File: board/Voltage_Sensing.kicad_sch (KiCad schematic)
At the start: 0 parts

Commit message: Schematics without values
Votlage Sensing circuit schematic
Oring controller circuit schematic
No values for components yet
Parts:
- added R10, R11, R12, R13, R14, R15, R16, R17, R18, R19, R20, R21, R22, R23, R24, R25, R26, R3, R4, R5, R6, R7, R8, R9: R_US, symbol Device:R_US
- added U4, U5, U6, U7, U8, U9: Opamp_Dual, symbol Device:Opamp_Dual
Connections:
- new net: R3.1, R4.2, U4.2 (-), U4.6 (-)
- new net: R13.1, R14.1, U6.3 (+)
- new net: R20.1, R22.1, U8.3 (+)
- new net: R23.1, R25.2, U9.2 (-)
- new net: R24.1, R26.1, U9.3 (+)
- new net: R7.1, R8.2, U5.2 (-)
- new net: R5.1, R6.1, U4.3 (+), U4.5 (+)
- new net: R10.1, R9.1, U5.3 (+)
- new net: R11.1, R12.2, U6.2 (-)
- new net: R19.1, R21.2, U8.2 (-)
- new net: R16.1, R17.1, U7.3 (+)
- new net: R15.1, R18.2, U7.2 (-)
- new net Cell_1: R5.2, R7.2
- new net Cell_2: R11.2, R9.2
- new net Cell_3: R13.2, R15.2
- new net Cell_4: R16.2, R19.2
- new net Cell_5: R20.2, R23.2
- new net Cell_6: R24.2
- new net Cell_Sense_1: R4.1, U4.1, U4.7
- new net Cell_Sense_2: R8.1, U5.1
- new net Cell_Sense_3: R12.1, U6.1
- new net Cell_Sense_4: R18.1, U7.1
- new net Cell_Sense_5: R21.1, U8.1
- new net Cell_Sense_6: R25.1, U9.1
- new net GND: R10.2, R14.2, R17.2, R22.2, R26.2, R3.2, R6.2

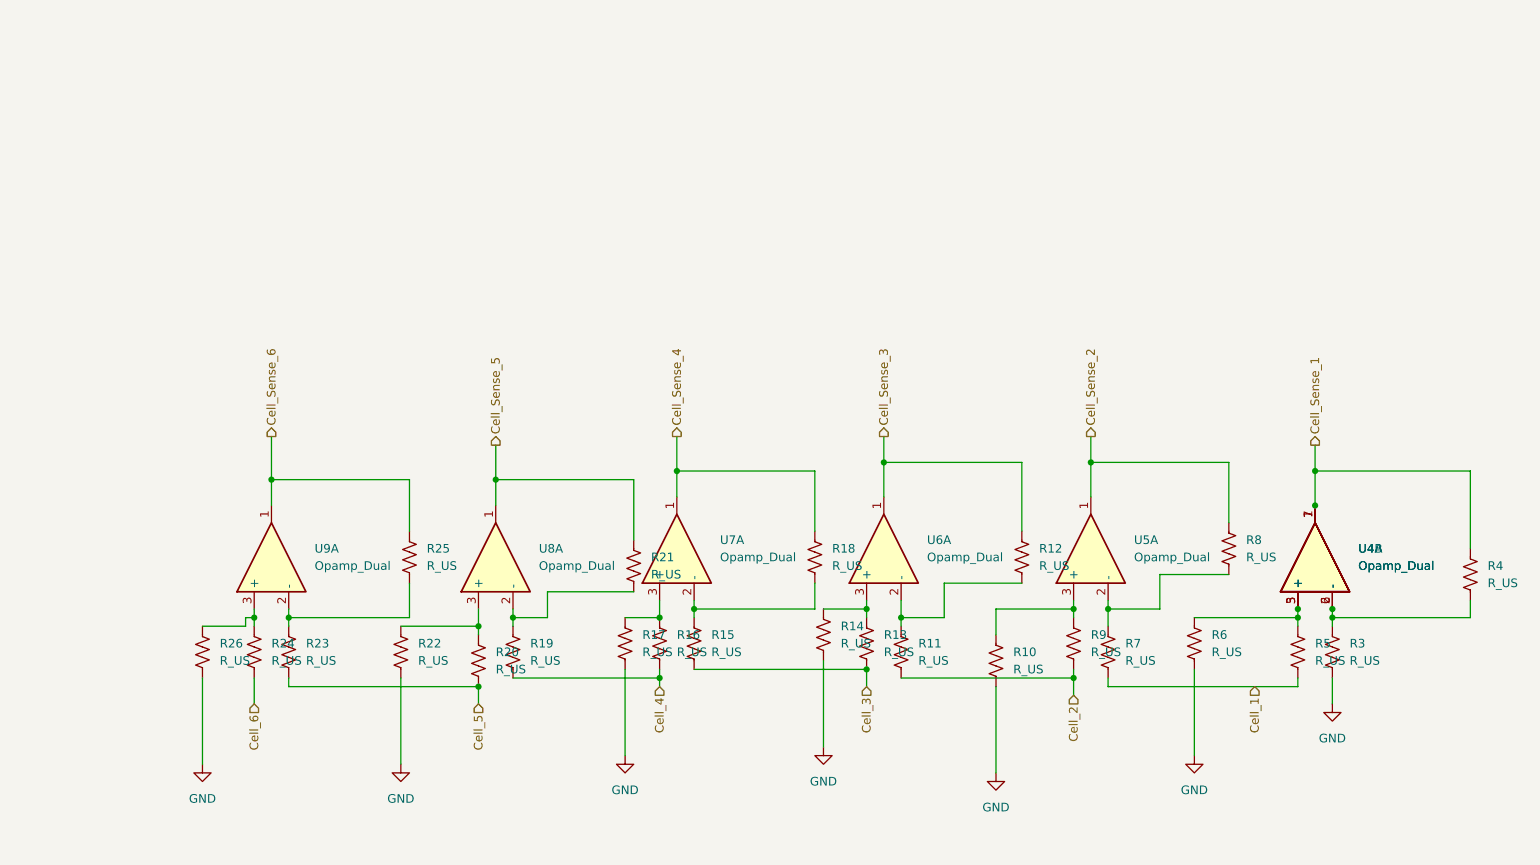
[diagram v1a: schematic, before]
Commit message: Added Zener DIodes
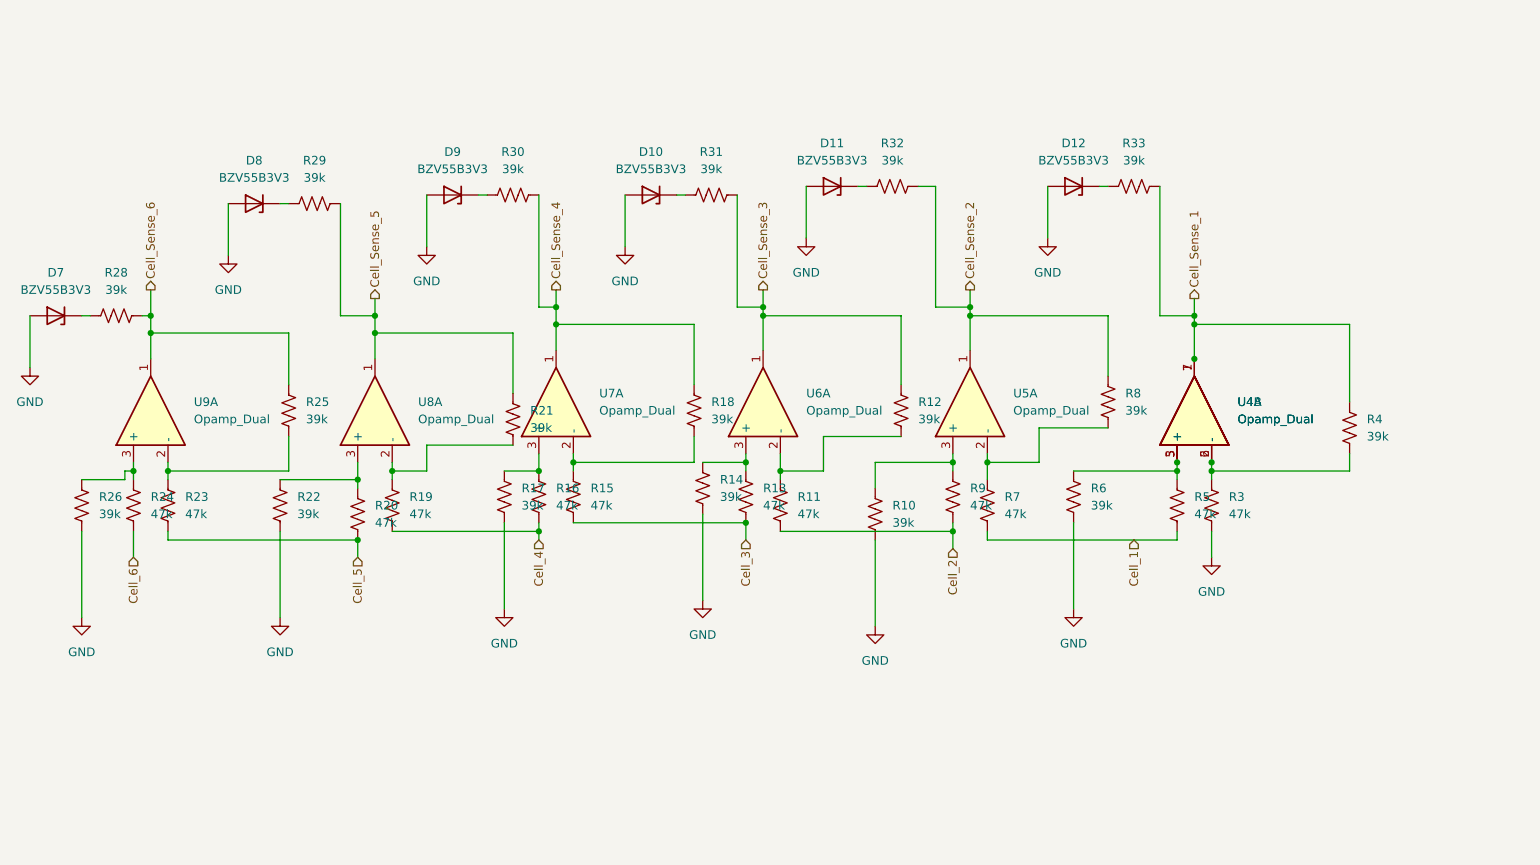
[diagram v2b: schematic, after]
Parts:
- added D10, D11, D12, D7, D8, D9: BZV55B3V3, Diode_SMD:D_MiniMELF, symbol Diode:BZV55B3V3
- added R28, R29, R30, R31, R32, R33: 39k, symbol Device:R_US
- R10, R12, R14, R17, R18, R21, R22, R25, R26, R4, R6, R8: value R_US -> 39k
- R11, R13, R15, R16, R19, R20, R23, R24, R3, R5, R7, R9: value R_US -> 47k
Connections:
- net Cell_Sense_1: now also R33.2
- net Cell_Sense_2: now also R32.2
- net Cell_Sense_3: now also R31.2
- net Cell_Sense_4: now also R30.2
- net Cell_Sense_5: now also R29.2
- net Cell_Sense_6: now also R28.2
- net GND: now also D10.2 (A), D11.2 (A), D12.2 (A), D7.2 (A), D8.2 (A), D9.2 (A)
- new net: D12.1 (K), R33.1
- new net: D11.1 (K), R32.1
- new net: D7.1 (K), R28.1
- new net: D10.1 (K), R31.1
- new net: D9.1 (K), R30.1
- new net: D8.1 (K), R29.1
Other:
- moved on the sheet: R10, R11, R12, R13, R14, R15, R16, R17, R18, R19, R20, R21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

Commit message: Changed Flags
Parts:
- D10, D11, D12, D8, D9: value BZV55B3V3 -> 3v3
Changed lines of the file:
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@@
 			)
 		)
-		(property "Value" "BZV55B3V3"
+		(property "Value" "3v3"
 			(at 161.29 43.18 0)
 			(effects
@@
 			)
 		)
-		(property "Value" "BZV55B3V3"
+		(property "Value" "3v3"
 			(at 134.62 44.45 0)
 			(effects
@@
 			)
 		)
-		(property "Value" "BZV55B3V3"
+		(property "Value" "3v3"
 			(at 105.41 44.45 0)
 			(effects
@@
 			)
 		)
-		(property "Value" "BZV55B3V3"
+		(property "Value" "3v3"
 			(at 196.85 43.18 0)
 			(effects
@@
 			)
 		)
-		(property "Value" "BZV55B3V3"
+		(property "Value" "3v3"
 			(at 76.2 45.72 0)
 			(effects

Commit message: added wiring and Voltage Sense Fix
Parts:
- renumbered R3 to R66
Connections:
- net Cell_Sense_1: now also D12.1 (K), R33.1; no longer R33.2, R4.1, U4.1, U4.7
- net Cell_Sense_2: now also D11.1 (K), R32.1; no longer R32.2, R8.1, U5.1
- net Cell_Sense_3: now also D10.1 (K), R31.1; no longer R12.1, R31.2, U6.1
- net Cell_Sense_5: now also D8.1 (K), R29.1; no longer R21.1, R29.2, U8.1
- net Cell_Sense_6: now also D7.1 (K), R28.1; no longer R25.1, R28.2, U9.1
- new net: R33.2, R4.1, U4.1, U4.7
- new net: R25.1, R28.2, U9.1
- new net: R32.2, R8.1, U5.1
- new net: R12.1, R31.2, U6.1
- new net: R21.1, R29.2, U8.1
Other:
- moved on the sheet: R33

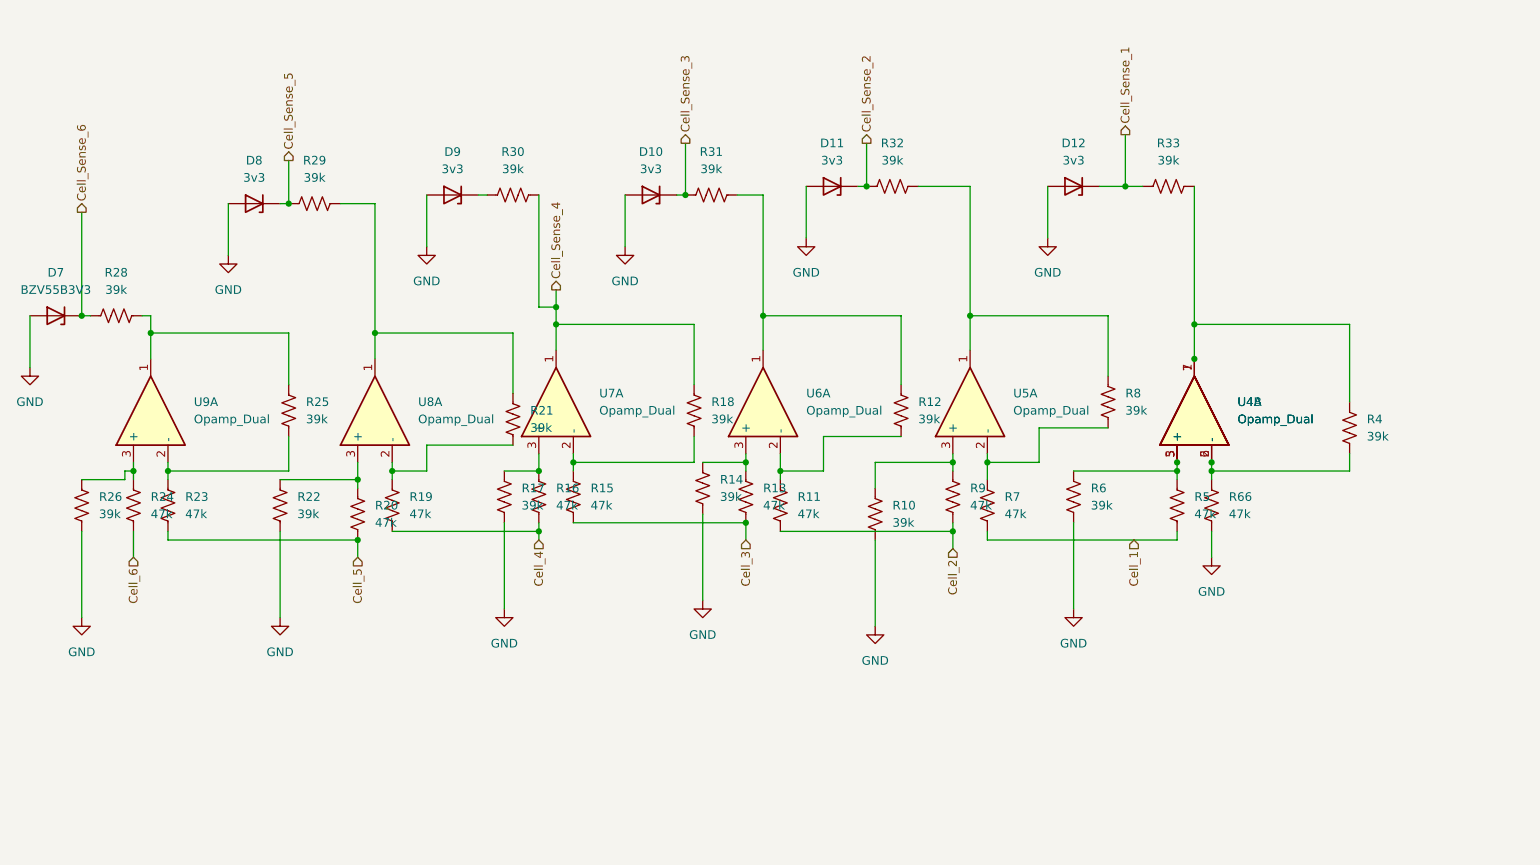
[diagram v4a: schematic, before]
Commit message: added port in voltage sensing
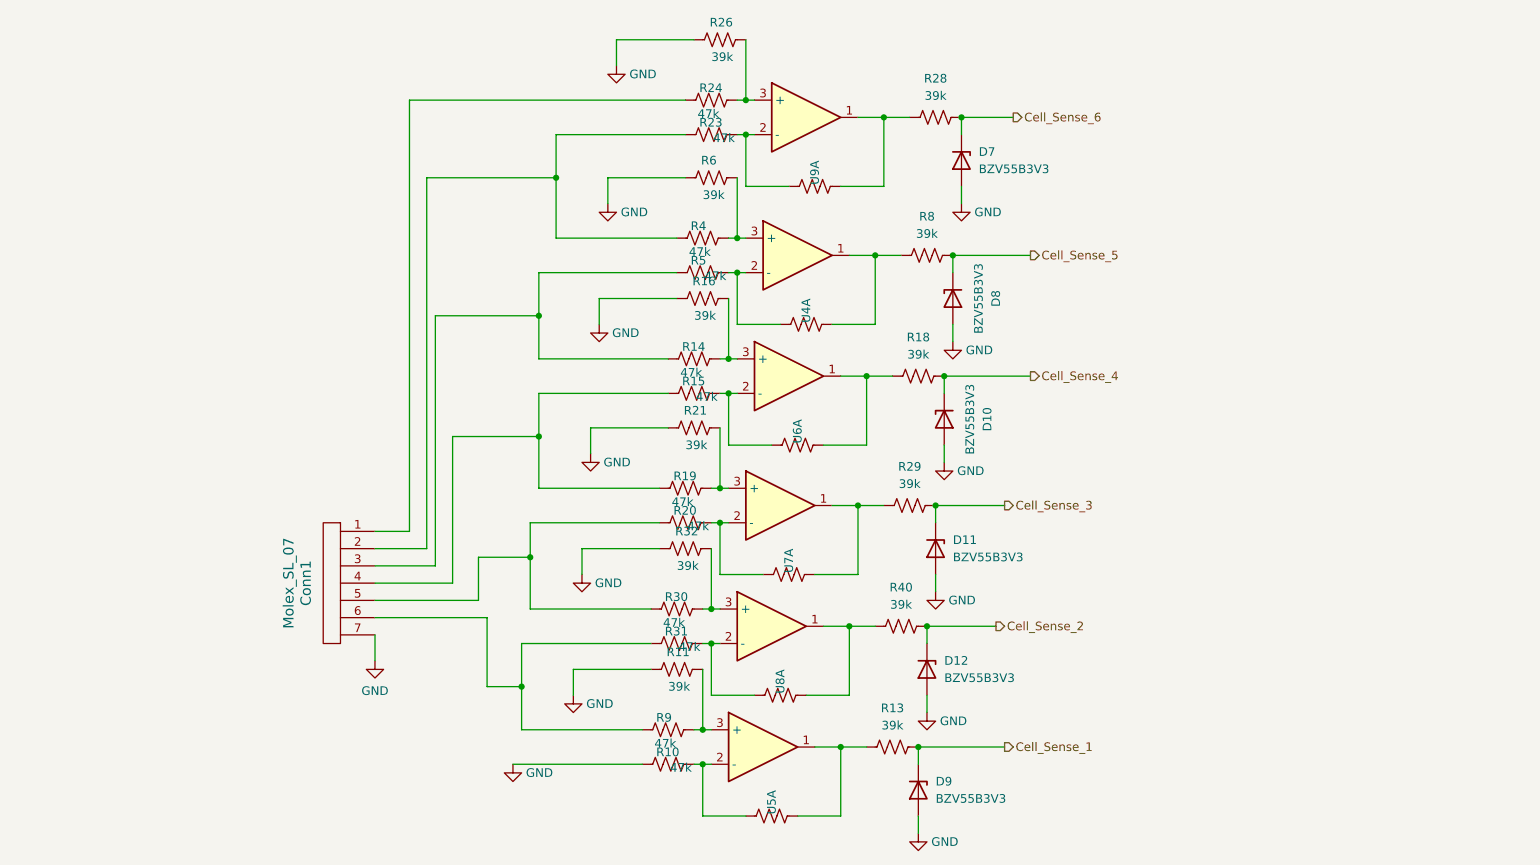
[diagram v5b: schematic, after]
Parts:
- removed R66: 47k, symbol Device:R_US
- removed unit 2 of U4
- added Conn1: Molex_SL_07, symbol MRDT_Connectors:Molex_SL_07
- added R40: 39k, symbol Device:R_US
- D10, D11, D12, D8, D9: value 3v3 -> BZV55B3V3
- R10, R14, R30, R31, R4: value 39k -> 47k
- R11, R13, R16, R7: value 47k -> 39k
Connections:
- net Cell_Sense_1: now also D9.1 (K), R13.2; no longer D12.1 (K), R33.1
- net Cell_Sense_2: now also D12.1 (K), R40.2; no longer D11.1 (K), R32.1
- net Cell_Sense_3: now also D11.1 (K), R29.2; no longer D10.1 (K), R31.1
- net Cell_Sense_4: now also D10.1 (K), R18.2; no longer R18.1, R30.2, U7.1
- net Cell_Sense_5: now also R8.2; no longer R29.1
- net Cell_Sense_6: now also R28.2; no longer R28.1
- net GND: now also R11.2, R16.2, R21.2, R32.2, Conn1.7; no longer R14.2, R17.2, R22.2
- net at U4.2 (-): now also R5.1, R7.2; no longer R4.2
- net at R14.1, U6.3 (+): now also R16.1; no longer R13.1
- net at R25.1, U9.1: now also R28.1; no longer R28.2
- net at R6.1, U4.3 (+): now also R4.1; no longer R5.1
- net at R9.1, U5.3 (+): now also R11.1; no longer R10.1
- net at R30.1: now also R32.1, U8.3 (+); no longer D9.1 (K)
- net Cell_1: no longer names the net of R5.2
- net Cell_1: now also R14.2, Conn1.3; no longer R7.2
- net Cell_2: no longer names the net of R9.2
- net Cell_2: now also R31.2, Conn1.6; no longer R11.2
- net Cell_3: no longer names the net of R15.2
- net Cell_3: now also R19.2, Conn1.4; no longer R13.2
- removed net Cell_4: R16.2, R19.2
- net Cell_5: no longer names the net of R20.2
- net Cell_5: now also R30.2, Conn1.5; no longer R23.2
- net Cell_6: no longer names the net of R24.2
- net Cell_6: now also Conn1.1
- new net: R33.1, R40.1, U8.1
- new net: R12.1, R13.1, U5.1
- new net: R10.1, R12.2, U5.2 (-)
- new net: R31.1, R33.2, U8.2 (-)
- new net: R7.1, R8.1, U4.1
- new net: R22.1, R29.1, U7.1
- new net: R20.1, R22.2, U7.2 (-)
- new net: R19.1, R21.1, U7.3 (+)
- new net: Conn1.2, R23.2, R4.2
- new net: R17.1, R18.1, U6.1
- new net: R15.1, R17.2, U6.2 (-)
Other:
- moved on the sheet: D7, R23, R24, R26, R28, U9A
